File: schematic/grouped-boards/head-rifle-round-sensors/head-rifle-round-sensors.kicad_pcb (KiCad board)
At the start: 2 copper layers, 126.5 x 95.1 mm, 209 parts, among them K1 CONN_3, K1 Power, K2 CONN_3, P1 MCU1, P1 SENSOR_CONNECTOR, P1 USB, P10 MCU2, P12 NRF24L01, P13 IR_LED, P15 Vibro&flash, P2 MCU1, P2 MICROSD-SDIO-CD, P2 VibroEngine, P2 Zone2, P3 MCU1, P3 Mag&fireMode, P3 SWD, P4 MCU2, P4 USART1, P4 VCC, P5 EXTENSION-CONNECTOR, P5 Speaker2, P6 MCU2, P6 UART1, P7 Fire&Reload, P8 EXTENSION-CONNECTOR, P8 NRF24L01, P9 Zone1, Q1 MOSFET_P, Q2 MOS_N, Q3 MOS_N, Q4 MOS_N, Q5 MOS_N, Q6 MOS_N, Q7 MOS_N, Q8 MOSFET_N, U1 NCP551, U1 PAM8403, U1 RGB-LED, U1 STM32F103RE, U2 NCP551, U2 RGB-LED, U2 USBLC6-4, U3 MCP73831, U3 TSOP4856, U3 USBLC6-4, U4 MCP73831, U4 TSOP4856, X1 32768Hz, X2 8MHz

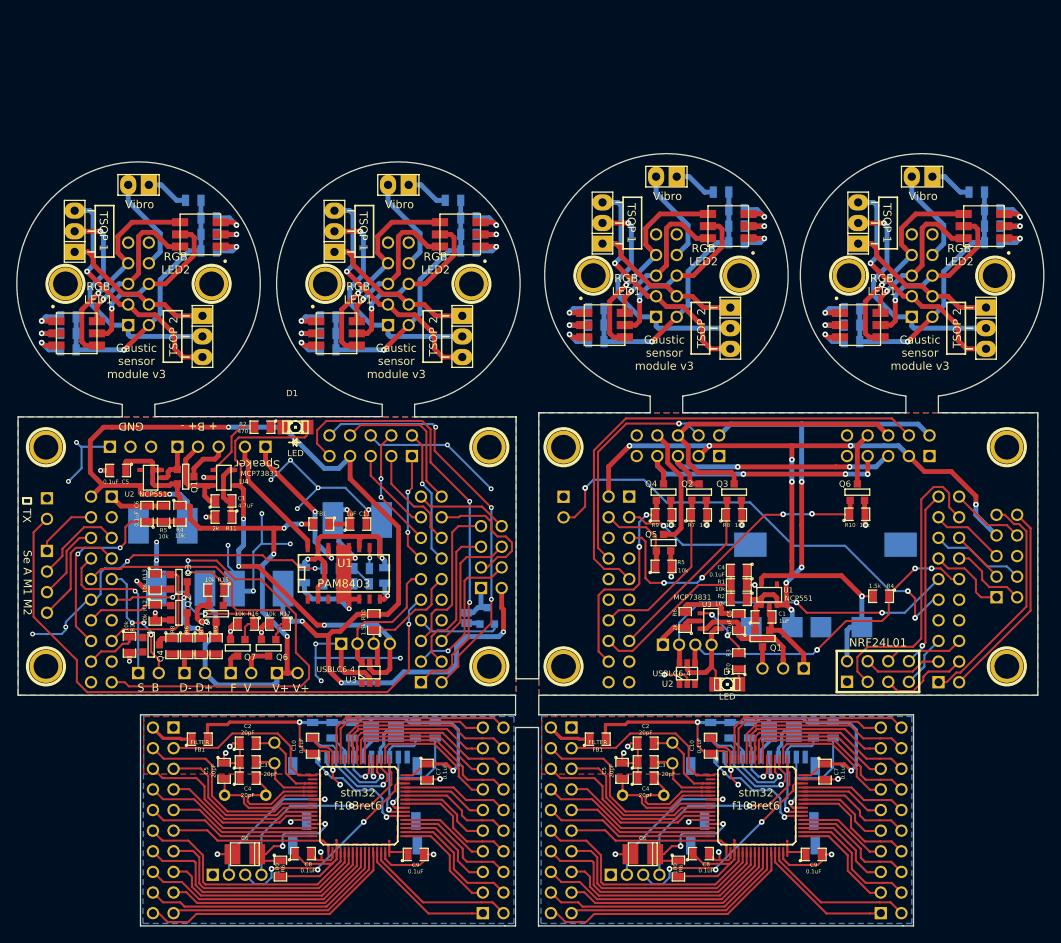
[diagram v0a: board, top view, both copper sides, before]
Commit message: Round sensor fix for TSOP orientation
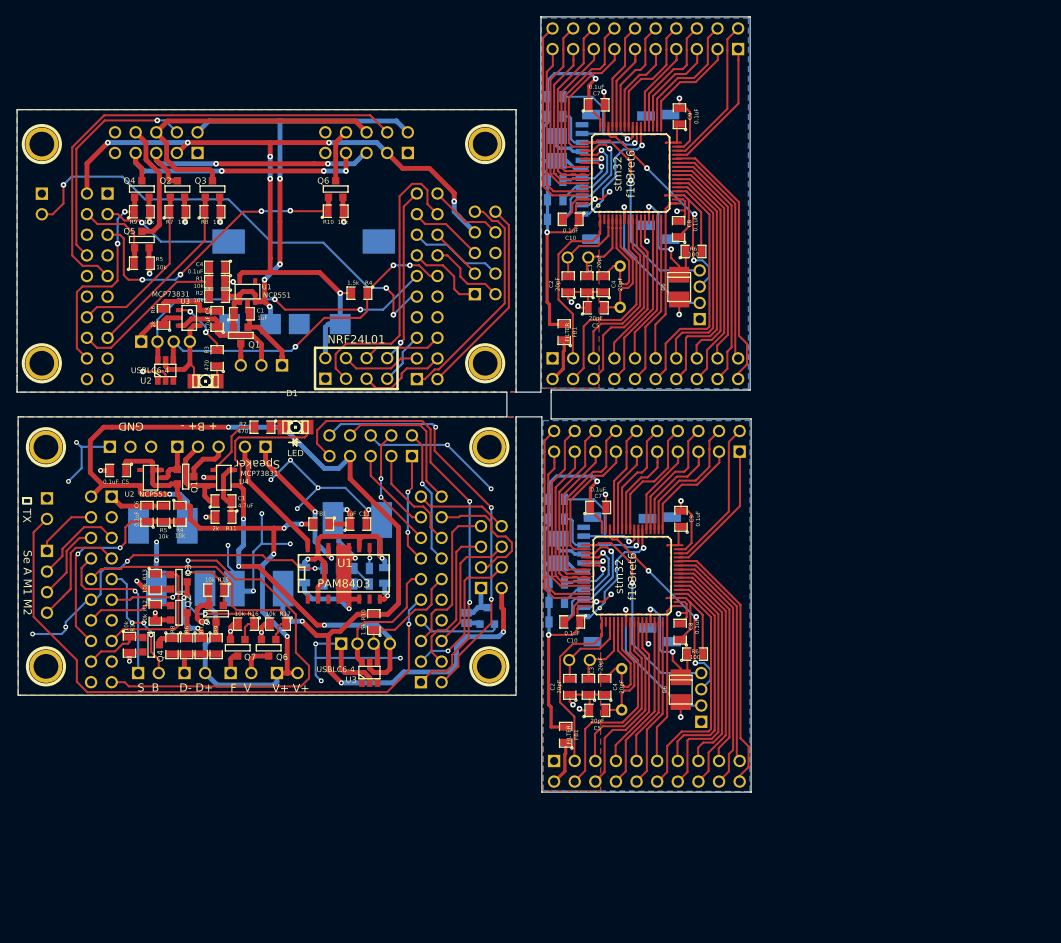
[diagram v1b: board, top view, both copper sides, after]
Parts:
- removed the 1PIN at (209.8, 132.5)
- removed the 1PIN at (162.8, 133.5)
- removed the 1PIN at (144.8, 133.5)
- removed the 1PIN at (227.8, 132.5)
- removed the 1PIN at (259.3, 132.5)
- removed the 1PIN at (241.3, 132.5)
- removed the 1PIN at (176.8, 133.5)
- removed the 1PIN at (194.8, 133.5)
- removed the C1 at (233.0, 188.7)
- removed the C1 at (183.9, 188.7)
- removed the C10 at (224.2, 190.4)
- removed the C10 at (175.2, 190.4)
- removed the C2 at (216.2, 190.1)
- removed the C2 at (167.2, 190.1)
- removed the C3 at (216.2, 192.4)
- removed the C3 at (167.2, 192.4)
- removed the C4 at (216.2, 194.4)
- removed the C4 at (167.2, 194.4)
- removed the C5 at (213.3, 193.5)
- removed the C5 at (164.3, 193.5)
- removed the C6 at (215.9, 203.7)
- removed the C6 at (166.9, 203.7)
- removed the C7 at (238.3, 193.6)
- removed the C7 at (189.3, 193.6)
- removed the C8 at (223.0, 203.7)
- removed the C8 at (174.0, 203.7)
- removed the C9 at (236.9, 203.8)
- removed the C9 at (187.9, 203.8)
- removed the FB1 at (210.3, 189.6)
- removed the FB1 at (161.3, 189.6)
- removed the P1 at (218.8, 132.5)
- removed the P1 at (250.3, 132.5)
- removed the P1 at (185.8, 133.5)
- removed the P1 at (205.8, 199.6)
- removed the P1 at (156.8, 199.6)
- removed the P1 at (153.8, 133.5)
- removed the P2 at (218.8, 120.3)
- removed the P2 at (250.3, 120.3)
- removed the P2 at (185.8, 121.3)
- removed the P2 at (229.3, 191.8)
- removed the P2 at (180.3, 191.8)
- removed the P2 at (153.8, 121.3)
- removed the P3 at (214.9, 206.3)
- removed the P3 at (165.9, 206.3)
- removed the P4 at (246.5, 199.6)
- removed the P4 at (197.5, 199.6)
- removed the R1 at (227.4, 128.4)
- removed the R1 at (258.9, 128.4)
- removed the R1 at (194.4, 129.4)
- removed the R1 at (226.6, 188.5)
- removed the R1 at (177.6, 188.5)
- removed the R1 at (162.4, 129.4)
- removed the R2 at (227.4, 126.4)
- removed the R2 at (258.9, 126.4)
- removed the R2 at (194.4, 127.4)
- removed the R2 at (224.2, 188.5)
- removed the R2 at (175.2, 188.5)
- removed the R2 at (162.4, 127.4)
- removed the R3 at (227.4, 124.3)
- removed the R3 at (258.9, 124.3)
- removed the R3 at (194.4, 125.3)
- removed the R3 at (239.3, 188.5)
- removed the R3 at (190.3, 188.5)
- removed the R3 at (162.4, 125.3)
- removed the R4 at (210.2, 136.5)
- removed the R4 at (241.7, 136.5)
- removed the R4 at (177.1, 137.5)
- removed the R4 at (236.9, 188.5)
- removed the R4 at (187.9, 188.5)
- removed the R4 at (145.1, 137.5)
- removed the R5 at (210.2, 138.6)
- removed the R5 at (241.7, 138.6)
- removed the R5 at (177.1, 139.6)
- removed the R5 at (229.0, 188.5)
- removed the R5 at (180.0, 188.5)
- removed the R5 at (145.1, 139.6)
- removed the R6 at (210.2, 140.6)
- removed the R6 at (241.7, 140.6)
- removed the R6 at (177.1, 141.6)
- removed the R6 at (220.3, 205.5)
- removed the R6 at (171.2, 205.5)
- removed the R6 at (145.1, 141.6)
- removed the R7 at (225.5, 122.2)
- removed the R7 at (257.0, 122.2)
- removed the R7 at (192.5, 123.2)
- removed the R7 at (160.5, 123.2)
- removed the U1 at (226.4, 126.4)
- removed the U1 at (257.9, 126.4)
- removed the U1 at (193.4, 127.4)
- removed the U1 at (229.9, 197.8)
- removed the U1 at (180.9, 197.8)
- removed the U1 at (161.4, 127.4)
- removed the U2 at (211.2, 138.6)
- removed the U2 at (242.7, 138.6)
- removed the U2 at (178.2, 139.6)
- removed the U2 at (146.2, 139.6)
- removed the U3 at (226.7, 138.9)
- removed the U3 at (258.2, 138.9)
- removed the U3 at (193.6, 140.0)
- removed the U3 at (161.6, 140.0)
- removed the U4 at (210.9, 126.0)
- removed the U4 at (242.4, 126.0)
- removed the U4 at (177.9, 127.0)
- removed the U4 at (145.9, 127.0)
- removed the X1 at (219.5, 191.3)
- removed the X1 at (170.5, 191.3)
- removed the X2 at (215.9, 196.5)
- removed the X2 at (166.9, 196.5)
- added C1: 100uF, c_tant_B, B.Cu at (205.5, 166.4)
- added C1: 100uF, c_tant_B, B.Cu at (205.3, 116.8)
- added C10: 0.1uF, SM0805, F.Cu at (207.2, 175.1)
- added C10: 0.1uF, SM0805, F.Cu at (207.0, 125.5)
- added C2: 20pF, SM0805, F.Cu at (206.9, 183.1)
- added C2: 20pF, SM0805, F.Cu at (206.7, 133.5)
- added C3: 20pF, SM0805, F.Cu at (209.2, 183.1)
- added C3: 20pF, SM0805, F.Cu at (209.0, 133.5)
- added C4: 20pF, SM0805, F.Cu at (211.2, 183.1)
- added C4: 20pF, SM0805, F.Cu at (211.0, 133.5)
- added C5: 20pF, SM0805, F.Cu at (210.3, 186.0)
- added C5: 20pF, SM0805, F.Cu at (210.1, 136.4)
- added C6: 100uF, c_tant_B, F.Cu at (220.6, 183.5)
- added C6: 100uF, c_tant_B, F.Cu at (220.4, 133.9)
- added C7: 0.1uF, SM0805, F.Cu at (210.4, 161.0)
- added C7: 0.1uF, SM0805, F.Cu at (210.2, 111.4)
- added C8: 0.1uF, SM0805, F.Cu at (220.5, 176.3)
- added C8: 0.1uF, SM0805, F.Cu at (220.3, 126.7)
- added C9: 0.1uF, SM0805, F.Cu at (220.6, 162.4)
- added C9: 0.1uF, SM0805, F.Cu at (220.4, 112.8)
- added FB1: FILTER, SM0805, F.Cu at (206.4, 189.0)
- added FB1: FILTER, SM0805, F.Cu at (206.2, 139.4)
- added P1: MCU1, pin_array_10x2, B.Cu at (216.4, 193.5)
- added P1: MCU1, pin_array_10x2, B.Cu at (216.2, 143.9)
- added P2: MICROSD-SDIO-CD, MICROSD-CD-112IJ, B.Cu at (208.6, 170.0)
- added P2: MICROSD-SDIO-CD, MICROSD-CD-112IJ, B.Cu at (208.4, 120.4)
- added P3: SWD, PIN_ARRAY-4X1-2mm-horiz, B.Cu at (223.1, 184.4)
- added P3: SWD, PIN_ARRAY-4X1-2mm-horiz, B.Cu at (222.9, 134.8)
- added P4: MCU2, pin_array_10x2, B.Cu at (216.4, 152.9)
- added P4: MCU2, pin_array_10x2, B.Cu at (216.2, 103.3)
- added R1: 47k, SM0805, B.Cu at (205.3, 172.7)
- added R1: 47k, SM0805, B.Cu at (205.1, 123.1)
- added R2: 47k, SM0805, B.Cu at (205.3, 175.1)
- added R2: 47k, SM0805, B.Cu at (205.1, 125.5)
- added R3: 47k, SM0805, B.Cu at (205.3, 160.0)
- added R3: 47k, SM0805, B.Cu at (205.1, 110.4)
- added R4: 47k, SM0805, B.Cu at (205.3, 162.4)
- added R4: 47k, SM0805, B.Cu at (205.1, 112.9)
- added R5: 47k, SM0805, B.Cu at (205.3, 170.3)
- added R5: 47k, SM0805, B.Cu at (205.1, 120.7)
- added R6: 100, SM0805, F.Cu at (222.3, 179.1)
- added R6: 100, SM0805, F.Cu at (222.1, 129.5)
- added U1: STM32F103RE, LQFP64-0.254mm-pins, F.Cu at (214.6, 169.4)
- added U1: STM32F103RE, LQFP64-0.254mm-pins, F.Cu at (214.4, 119.8)
- added X1: 32768Hz, TC26H-fixed, B.Cu at (208.1, 179.8)
- added X1: 32768Hz, TC26H-fixed, B.Cu at (207.9, 130.2)
- added X2: 8MHz, HC-49V, B.Cu at (213.3, 183.4)
- added X2: 8MHz, HC-49V, B.Cu at (213.1, 133.8)
- moved C5 74.3 mm to (163.4, 137.8)
- moved K1 74.3 mm to (168.9, 143.5)
- moved P8 74.3 mm to (180.6, 143.9)
- moved Q5 74.3 mm to (154.2, 128.0)
- moved R10 74.3 mm to (178.1, 124.5)
- moved R8 74.3 mm to (162.9, 124.6)
- moved R9 74.3 mm to (154.2, 124.6)
- moved U1 74.3 mm to (167.2, 134.4)
- moved 1PIN 74.3 mm to (141.9, 143.3)
- moved 1PIN 74.3 mm to (141.9, 116.3)
- moved 1PIN 74.3 mm to (196.5, 116.3)
- moved 1PIN 74.3 mm to (196.5, 143.3)
- moved BT1 74.3 mm to (174.4, 128.3)
- moved C2 74.3 mm to (167.5, 138.4)
- moved C3 74.3 mm to (176.1, 138.4)
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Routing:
- net +BATT: track 149.0 -> 16.3 mm, vias 5 -> 1
- net +3.3V: track 515.0 -> 397.0 mm, vias 20 -> 16
- net GND: track 421.0 -> 304.6 mm, vias 58 -> 54
- net N-0000014: track 152.6 -> 47.4 mm, vias 5 -> 1
- net N-0000013: track 137.6 -> 50.1 mm, vias 4 -> 0
- net N-000003: track 159.3 -> 81.2 mm
- net N-0000012: track 160.3 -> 83.1 mm, vias 6 -> 2
- net N-000007: track 144.0 -> 96.5 mm
- net N-000008: track 140.5 -> 119.4 mm
- net N-0000016: track 75.6 -> 55.9 mm, vias 4 -> 0
- net N-000004: track 96.7 -> 77.9 mm, vias 4 -> 0
- net N-0000015: track 96.3 -> 77.7 mm, vias 5 -> 1
- net N-0000017: track 68.0 -> 50.3 mm, vias 4 -> 0
- net N-000006: track 59.2 -> 41.6 mm, vias 4 -> 0
- net N-000005: track 88.3 -> 71.6 mm, vias 6 -> 2
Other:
- board size 126.5 x 95.1 mm -> 90.4 x 95.5 mm
- board text removed: "Caustic sensor module v3"
- board text removed: "RGB LED1"
- board text removed: "RGB LED2"
- board text removed: "TSOP 1"
- board text removed: "TSOP 2"
